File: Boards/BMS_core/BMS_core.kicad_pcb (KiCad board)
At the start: 2 copper layers, 31 parts, among them IC1 ATMEGA16M1, J1 CONN_02X03, T1 T_LAN_7490100111A, U1 MCP2561-E_SN, U101 TPS561201, Y1 Crystal_SMD

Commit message: Rev 1 Layout of BMS Core
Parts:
- added C10: C_0.1uF, footprints:C_0805_OEM, F.Cu at (107.6, 57.5)
- added C6: C_0.1uF, footprints:C_0805_OEM, F.Cu at (64.5, 81.8)
- added C7: C_0.1uF, footprints:C_0805_OEM, F.Cu at (97.3, 57.7)
- added C8: C_10nF, footprints:C_0805_OEM, F.Cu at (82.0, 104.6)
- added C9: C_10nF, footprints:C_0805_OEM, F.Cu at (85.6, 102.6)
- added D1: LED_0805, footprints:LED_0805_OEM, F.Cu at (77.0, 67.5)
- added D2: LED_0805, footprints:LED_0805_OEM, F.Cu at (77.0, 69.8)
- added D3: LED_0805, footprints:LED_0805_OEM, F.Cu at (77.0, 72.4)
- added D4: BAS40-00, Package_TO_SOT_SMD:SOT-23, F.Cu at (84.8, 59.2)
- added J2: B5B-PH-K-S, footprints:B5B-PH-K-S, F.Cu at (98.3, 52.6)
- added J3: NanoFit_2, footprints:NanoFit_Molex_1x02x2.50mm_Angled_OEM, F.Cu at (104.1, 95.2)
- added J4: MicroFit_RA_R_2, footprints:MicroFit_RA_2, F.Cu at (49.5, 57.1)
- added J5: MM_F_VT_14, footprints:micromatch_female_vert_14, F.Cu at (45.7, 72.4)
- added K1: G5Q-1A4-DC5-5V, footprints:Relay_SPST_OMRON-G5Q-1A4_OEM, F.Cu at (81.3, 52.1)
- added Q1: SSM3K333R, footprints:SOT-23F, F.Cu at (85.3, 52.7)
- added R10: R_60.4, footprints:R_0805_OEM, F.Cu at (85.6, 104.6)
- added R11: R_60.4, footprints:R_0805_OEM, F.Cu at (85.6, 100.6)
- added R12: R_10K, footprints:R_0805_OEM, F.Cu at (88.4, 52.7)
- added R13: R_17.4K_0.1, footprints:R_0805_OEM, F.Cu at (101.6, 61.7)
- added R14: R_1K_0.1, footprints:R_0805_OEM, F.Cu at (103.6, 61.7)
- added R4: R_200, footprints:R_0805_OEM, F.Cu at (73.3, 67.5)
- added R5: R_200, footprints:R_0805_OEM, F.Cu at (73.3, 69.8)
- added R6: R_200, footprints:R_0805_OEM, F.Cu at (73.3, 72.3)
- added R7: R_10K, footprints:R_0805_OEM, F.Cu at (91.1, 56.9)
- added R8: R_3.01K, footprints:R_0805_OEM, F.Cu at (82.5, 95.6)
- added R9: R_1K, footprints:R_0805_OEM, F.Cu at (80.7, 97.6)
- added REF**: Bolt_connect_4-40_round, footprints:Bolt_connect_4-40_round, F.Cu at (112.4, 52.7)
- added REF**: Bolt_connect_4-40_round, footprints:Bolt_connect_4-40_round, F.Cu at (47.6, 104.8)
- added REF**: Bolt_connect_4-40_round, footprints:Bolt_connect_4-40_round, F.Cu at (112.4, 104.8)
- added U2: SN74LVC1G17, Package_TO_SOT_SMD:SOT-23-5, F.Cu at (61.5, 81.8)
- added U3: LTC6820HMS, Package_SO:MSOP-16_3x4mm_P0.5mm, F.Cu at (79.4, 91.2)
- added U4: MCP6001, footprints:SOT-23-5_OEM, F.Cu at (100.3, 57.7)
- added U5: MCP6001, footprints:SOT-23-5_OEM, F.Cu at (107.5, 60.5)
- R104: value R_51.1K -> R_54.9K
- moved R3 89.2 mm to (53.3, 70.4), turned to 90 degrees
- moved U101 80.3 mm to (61.8, 102.7)
- moved C101 80.3 mm to (58.4, 103.0)
- moved C102 80.3 mm to (64.8, 104.0)
- moved C103 80.3 mm to (68.6, 93.3)
- moved C104 80.3 mm to (68.6, 95.4)
- moved C105 80.3 mm to (68.6, 97.7)
- moved D102 80.3 mm to (51.6, 95.6)
- moved L101 80.3 mm to (61.8, 96.1)
- moved R101 80.3 mm to (52.3, 99.2)
- moved R102 80.3 mm to (52.3, 101.2)
- moved R103 80.3 mm to (59.9, 106.3)
- moved D101 80.3 mm to (54.1, 89.0)
- moved D103 80.3 mm to (64.3, 86.5)
- moved F101 80.3 mm to (55.5, 96.8)
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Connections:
- net /12V_Fused renamed Net-(C101-Pad1)
- IC1 pad 13: Net-(IC1-Pad13) -> /PROG_1
- IC1 pad 14: Net-(IC1-Pad14) -> /PROG_2
- IC1 pad 15: Net-(IC1-Pad15) -> /PROG_3
- IC1 pad 16: Net-(IC1-Pad16) -> /~OCD
- IC1 pad 17: Net-(IC1-Pad17) -> /VREF
- IC1 pad 18: Net-(IC1-Pad18) -> /VOUT
- IC1 pad 22: /SensorAmp -> /BMS_SENSE
- IC1 pad 25: Net-(IC1-Pad25) -> /RELAY_DRIVE
- IC1 pad 27: Net-(IC1-Pad27) -> /CS_iso
- IC1 pad 28: Net-(IC1-Pad28) -> /SCK_iso
- IC1 pad 3: /SS -> /FAN_PWM_RAW
- IC1 pad 30: Net-(IC1-Pad30) -> /BSPD_CURRENT
- IC1 pad 8: Net-(IC1-Pad8) -> /MISO_iso
- IC1 pad 9: Net-(IC1-Pad9) -> /MOSI_iso
- R1 pad 1: Net-(R1-Pad1) -> VCC
- R104 pad 1: Net-(C103-Pad1) -> Net-(R103-Pad1)
- R104 pad 2: Net-(R103-Pad1) -> Net-(C103-Pad1)
- R3 pad 1: Net-(R3-Pad1) -> /CANH
- R3 pad 2: Net-(R3-Pad2) -> /CANL
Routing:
- net VCC: track 4.46 -> 212.2 mm, vias 0 -> 5
- net /VOUT: track 0.00 -> 81.4 mm, vias 0 -> 4
- net /BSPD_CURRENT: track 0.00 -> 78.4 mm, vias 0 -> 4
- net +12V: track 4.95 -> 79.7 mm
- net /MISO: track 0.00 -> 73.4 mm, vias 0 -> 3
- net /RESET: track 0.00 -> 70.8 mm, vias 0 -> 4
- net /MOSI: track 0.00 -> 69.8 mm, vias 0 -> 3
- net /SCK: track 0.00 -> 64.6 mm, vias 0 -> 5
- net /VREF: track 0.00 -> 59.5 mm, vias 0 -> 2
- net GND: track 14.4 -> 70.8 mm, vias 14 -> 39
- net /TXCAN: track 0.00 -> 52.1 mm
- net /RXCAN: track 0.00 -> 42.6 mm
- net /BMS_SENSE: track 0.00 -> 40.7 mm, vias 0 -> 2
- net /~OCD: track 0.00 -> 39.7 mm, vias 0 -> 2
- net /FAN_PWM_RAW: track 0.00 -> 35.6 mm, vias 0 -> 2
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- added copper zone on B.Cu, net GND
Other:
- board outline added: 73.7 x 61 mm
- board text added: "GLV"
- board text added: "HV"
- board text added: "MKIV BMS Core Rev 1.0 Olin Electric Motorsports Alexander Hoppe '19"
- board text added: "PD5"
- board text added: "PD6"
- board text added: "PD7"

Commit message: Add gerbers for BMS Core Rev.1
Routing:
- net /SHDN_OUT(BMS->IMD): track 0.00 -> 19.9 mm
- net /SHDN_IN(MAIN_PACK->BMS): track 0.00 -> 12.4 mm
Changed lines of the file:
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@@
     (thickness 1.6)
     (drawings 16)
-    (tracks 726)
+    (tracks 732)
     (zones 0)
     (modules 64)
@@
   )
   (setup
-    (last_trace_width 0.254)
+    (last_trace_width 0.762)
     (user_trace_width 0.1524)
     (user_trace_width 0.254)
@@
   (segment (start 77.654257 78.852742) (end 78.546757 77.960242) (width 0.254) (layer F.Cu) (net 15))
   (segment (start 77.654257 78.963742) (end 77.654257 78.852742) (width 0.254) (layer F.Cu) (net 15))
-  (segment (start 59.0101 101.5795) (end 58.9601 101.6295) (width 0.6) (layer F.Cu) (net 38) (status 30))
   (segment (start 54.2925 91.059) (end 54.102 91.059) (width 0.254) (layer F.Cu) (net 16))
   (segment (start 55.4795 92.246) (end 54.2925 91.059) (width 0.254) (layer F.Cu) (net 16))
@@
   (segment (start 83.82 104.648) (end 83.042 104.648) (width 0.254) (layer F.Cu) (net 36))
   (segment (start 90.26 102.616) (end 86.598 102.616) (width 0.254) (layer F.Cu) (net 37))
+  (segment (start 59.0101 101.5795) (end 58.9601 101.6295) (width 0.6) (layer F.Cu) (net 38) (status 30))
   (segment (start 78.700757 67.533742) (end 78.135257 67.533742) (width 0.254) (layer F.Cu) (net 39))
   (segment (start 84.255257 73.088242) (end 78.700757 67.533742) (width 0.254) (layer F.Cu) (net 39))
@@
   (segment (start 100.544 101.346) (end 99.06 101.346) (width 0.254) (layer F.Cu) (net 56))
   (segment (start 104.14 97.75) (end 100.544 101.346) (width 0.254) (layer F.Cu) (net 56))
-  (segment (start 101.536001 51.816001) (end 102.298 52.578) (width 0.254) (layer F.Cu) (net 69))
-  (segment (start 90.17 56.896) (end 90.17 54.864) (width 0.254) (layer F.Cu) (net 69))
-  (segment (start 90.17 54.864) (end 93.726 51.308) (width 0.254) (layer F.Cu) (net 69))
-  (segment (start 93.726 51.308) (end 101.028 51.308) (width 0.254) (layer F.Cu) (net 69))
-  (segment (start 101.028 51.308) (end 101.536001 51.816001) (width 0.254) (layer F.Cu) (net 69))
-  (segment (start 90.17 56.896) (end 90.17 60.452) (width 0.254) (layer F.Cu) (net 69))
-  (segment (start 90.17 60.452) (end 90.17 60.96) (width 0.254) (layer F.Cu) (net 69))
-  (via (at 84.074 62.23) (size 0.6096) (drill 0.3048) (layers F.Cu B.Cu) (net 69))
-  (segment (start 90.17 60.96) (end 88.9 62.23) (width 0.254) (layer F.Cu) (net 69))
-  (segment (start 88.9 62.23) (end 84.074 62.23) (width 0.254) (layer F.Cu) (net 69))
-  (segment (start 84.074 62.23) (end 84.074 62.992) (width 0.254) (layer B.Cu) (net 69))
-  (segment (start 84.074 62.992) (end 81.788 65.278) (width 0.254) (layer B.Cu) (net 69))
-  (via (at 81.788 72.644) (size 0.6096) (drill 0.3048) (layers F.Cu B.Cu) (net 69))
-  (segment (start 81.788 65.278) (end 81.788 72.644) (width 0.254) (layer B.Cu) (net 69))
+  (segment (start 56.92 58.65) (end 53.85 58.65) (width 0.762) (layer F.Cu) (net 57))
+  (segment (start 63.5 52.07) (end 56.92 58.65) (width 0.762) (layer F.Cu) (net 57))
+  (segment (start 54.559999 54.940001) (end 53.85 55.65) (width 0.762) (layer F.Cu) (net 58))
+  (segment (start 58.863401 50.636599) (end 54.559999 54.940001) (width 0.762) (layer F.Cu) (net 58))
+  (segment (start 69.686599 50.636599) (end 58.863401 50.636599) (width 0.762) (layer F.Cu) (net 58))
+  (segment (start 71.12 52.07) (end 69.686599 50.636599) (width 0.762) (layer F.Cu) (net 58))
   (segment (start 48.26 82.296) (end 50.292 84.328) (width 0.254) (layer F.Cu) (net 61))
   (segment (start 50.292 84.328) (end 56.642 84.328) (width 0.254) (layer F.Cu) (net 61))
@@
   (segment (start 81.959166 52.749166) (end 81.28 52.07) (width 0.762) (layer F.Cu) (net 68))
   (segment (start 84.294147 52.749166) (end 81.959166 52.749166) (width 0.762) (layer F.Cu) (net 68))
+  (segment (start 101.536001 51.816001) (end 102.298 52.578) (width 0.254) (layer F.Cu) (net 69))
+  (segment (start 90.17 56.896) (end 90.17 54.864) (width 0.254) (layer F.Cu) (net 69))
+  (segment (start 90.17 54.864) (end 93.726 51.308) (width 0.254) (layer F.Cu) (net 69))
+  (segment (start 93.726 51.308) (end 101.028 51.308) (width 0.254) (layer F.Cu) (net 69))
+  (segment (start 101.028 51.308) (end 101.536001 51.816001) (width 0.254) (layer F.Cu) (net 69))
+  (segment (start 90.17 56.896) (end 90.17 60.452) (width 0.254) (layer F.Cu) (net 69))
+  (segment (start 90.17 60.452) (end 90.17 60.96) (width 0.254) (layer F.Cu) (net 69))
+  (via (at 84.074 62.23) (size 0.6096) (drill 0.3048) (layers F.Cu B.Cu) (net 69))
+  (segment (start 90.17 60.96) (end 88.9 62.23) (width 0.254) (layer F.Cu) (net 69))
+  (segment (start 88.9 62.23) (end 84.074 62.23) (width 0.254) (layer F.Cu) (net 69))
+  (segment (start 84.074 62.23) (end 84.074 62.992) (width 0.254) (layer B.Cu) (net 69))
+  (segment (start 84.074 62.992) (end 81.788 65.278) (width 0.254) (layer B.Cu) (net 69))
+  (via (at 81.788 72.644) (size 0.6096) (drill 0.3048) (layers F.Cu B.Cu) (net 69))
+  (segment (start 81.788 65.278) (end 81.788 72.644) (width 0.254) (layer B.Cu) (net 69))
   (segment (start 81.855257 72.711257) (end 81.788 72.644) (width 0.254) (layer F.Cu) (net 69))
   (segment (start 81.855257 74.142242) (end 81.855257 72.711257) (width 0.254) (layer F.Cu) (net 69))

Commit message: Add silkscreens and update gerbers for rev 1
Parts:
- added G***: LOGO, footprints:Olin_O, B.Cu at (92.3, 55.9)
- moved G*** 78.5 mm to (80.8, 102.8), turned to 180 degrees
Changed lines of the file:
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@@
     (tracks 732)
     (zones 0)
-    (modules 64)
+    (modules 65)
     (nets 70)
   )
@@
     (34 B.Paste user)
     (35 F.Paste user)
-    (36 B.SilkS user hide)
+    (36 B.SilkS user)
     (37 F.SilkS user)
-    (38 B.Mask user)
+    (38 B.Mask user hide)
     (39 F.Mask user hide)
     (40 Dwgs.User user)
@@
   )
   (setup
-    (last_trace_width 0.762)
+    (last_trace_width 0.1524)
     (user_trace_width 0.1524)
     (user_trace_width 0.254)
@@
       (drillshape 0)
       (scaleselection 1)
-      (outputdirectory "Gerb_new/"))
+      (outputdirectory "gerbers/"))
   )
   (net 0 "")
@@
   )
   (module footprints:Logo_Large (layer B.Cu)
-    (at 159.004 109.728)
-    (fp_text reference G*** (at 0 0) (layer B.SilkS) hide
+    (at 80.8482 102.7938 180)
+    (fp_text reference G*** (at 0 0 180) (layer B.SilkS) hide
       (effects (font (size 1.524 1.524) (thickness 0.3)) (justify mirror))
     )
-    (fp_text value LOGO (at 0.75 0) (layer B.SilkS) hide
+    (fp_text value LOGO (at 0.75 0 180) (layer B.SilkS) hide
       (effects (font (size 1.524 1.524) (thickness 0.3)) (justify mirror))
     )
@@
       (clearance 0.508))
   )
+  (module footprints:Olin_O (layer B.Cu)
+    (at 92.329 55.8546)
+    (fp_text reference G*** (at 10.16 5.08) (layer B.SilkS) hide
+      (effects (font (size 1.524 1.524) (thickness 0.3)) (justify mirror))
+    )
+    (fp_text value LOGO (at 10.16 7.62) (layer B.SilkS) hide
+      (effects (font (size 1.524 1.524) (thickness 0.3)) (justify mirror))
+    )
+    (fp_poly (pts (xy 0.78907 2.933726) (xy 0.297169 2.603291) (xy -0.249654 2.169905) (xy -0.811 1.670573)
+      (xy -1.346471 1.1423) (xy -1.815667 0.622091) (xy -2.036037 0.345931) (xy -2.493304 -0.320664)
+      (xy -2.866143 -0.986545) (xy -3.148527 -1.632052) (xy -3.33443 -2.237523) (xy -3.417825 -2.783297)
+      (xy -3.392687 -3.249711) (xy -3.252989 -3.617104) (xy -3.251451 -3.6195) (xy -3.169272 -3.757194)
+      (xy -3.151881 -3.805837) (xy -3.238357 -3.784085) (xy -3.451232 -3.729169) (xy -3.753084 -3.650766)
+      (xy -3.937 -3.602827) (xy -4.929803 -3.301284) (xy -5.762117 -2.955854) (xy -6.437575 -2.564339)
+      (xy -6.959808 -2.124543) (xy -7.332449 -1.634266) (xy -7.40086 -1.507176) (xy -7.582592 -0.976433)
+      (xy -7.604253 -0.451032) (xy -7.475103 0.063274) (xy -7.204403 0.560731) (xy -6.801416 1.035585)
+      (xy -6.275401 1.482082) (xy -5.63562 1.894469) (xy -4.891334 2.266991) (xy -4.051805 2.593894)
+      (xy -3.126293 2.869426) (xy -2.12406 3.087831) (xy -1.054367 3.243355) (xy 0.073526 3.330246)
+      (xy 0.403482 3.341618) (xy 1.526631 3.369785) (xy 0.78907 2.933726)) (layer B.SilkS) (width 0.01))
+    (fp_poly (pts (xy 3.442983 3.189143) (xy 3.593457 3.149129) (xy 3.859628 3.080824) (xy 4.192829 2.996675)
+      (xy 4.318 2.965353) (xy 4.950523 2.771412) (xy 5.589166 2.511366) (xy 6.187709 2.208074)
+      (xy 6.699928 1.884399) (xy 7.006464 1.635631) (xy 7.427728 1.15255) (xy 7.68721 0.655705)
+      (xy 7.791208 0.151883) (xy 7.746021 -0.352128) (xy 7.557949 -0.849541) (xy 7.23329 -1.333569)
+      (xy 6.778343 -1.797426) (xy 6.199408 -2.234324) (xy 5.502783 -2.637476) (xy 4.694767 -3.000096)
+      (xy 3.78166 -3.315395) (xy 2.769759 -3.576588) (xy 2.037525 -3.718298) (xy 1.579989 -3.791873)
+      (xy 1.263227 -3.832252) (xy 1.062288 -3.841026) (xy 0.952225 -3.819783) (xy 0.916988 -3.789688)
+      (xy 0.858074 -3.735928) (xy 0.847963 -3.779733) (xy 0.766319 -3.839404) (xy 0.537525 -3.878973)
+      (xy 0.3175 -3.891838) (xy -0.049381 -3.903054) (xy -0.420533 -3.915266) (xy -0.613858 -3.922106)
+      (xy -0.848176 -3.919314) (xy -0.993137 -3.895498) (xy -1.016025 -3.876157) (xy -1.081706 -3.846379)
+      (xy -1.164166 -3.861997) (xy -1.171663 -3.848862) (xy -1.054877 -3.771153) (xy -0.838402 -3.644985)
+      (xy -0.801282 -3.624227) (xy -0.008948 -3.11414) (xy 0.773964 -2.467576) (xy 1.356472 -1.894766)
+      (xy 2.033545 -1.129263) (xy 2.578075 -0.383663) (xy 3.016751 0.379744) (xy 3.126149 0.605915)
+      (xy 3.414204 1.311966) (xy 3.572957 1.91735) (xy 3.603305 2.429665) (xy 3.50615 2.856508)
+      (xy 3.413505 3.034819) (xy 3.334494 3.173405) (xy 3.358577 3.208225) (xy 3.442983 3.189143)) (layer B.SilkS) (width 0.01))
+  )
   (gr_arc (start 45.72 106.68) (end 43.18 106.68) (angle -90) (layer Edge.Cuts) (width 0.15))

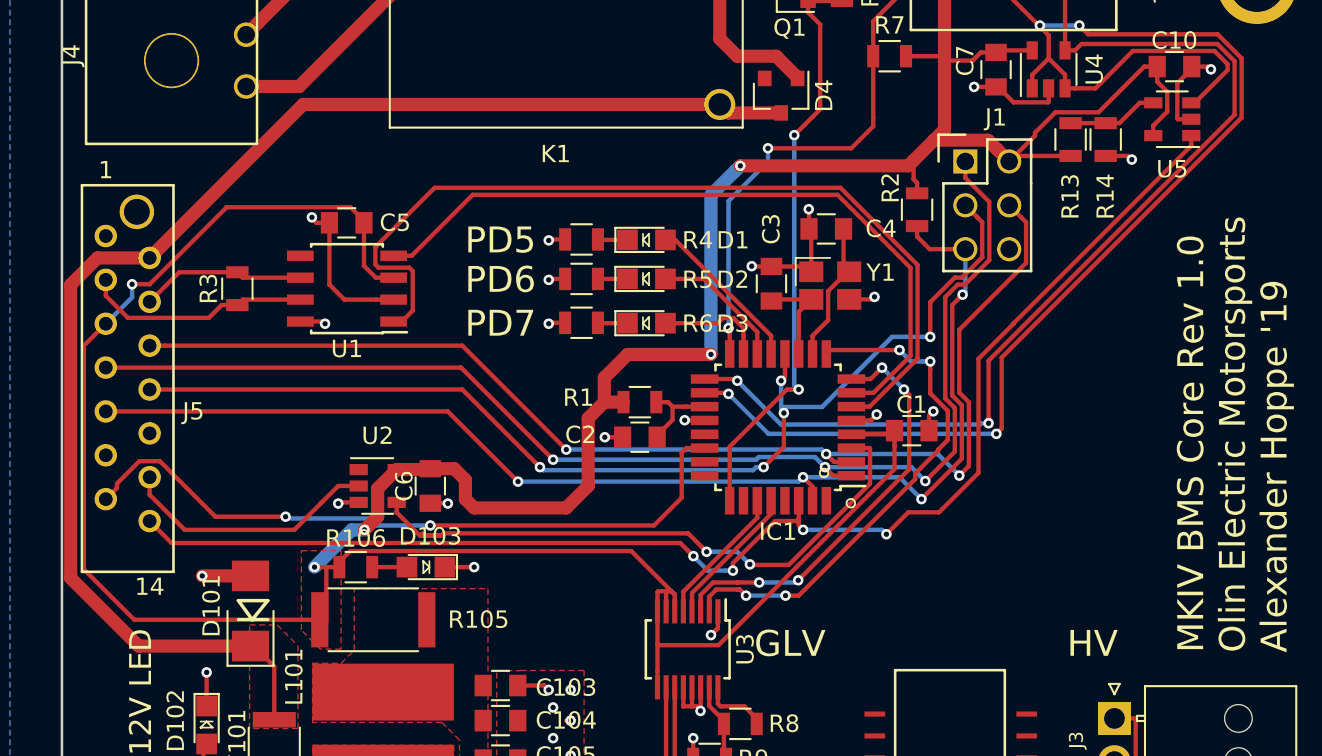
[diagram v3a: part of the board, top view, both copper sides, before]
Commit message: Update BMS Core with LED1 and LED2 connections
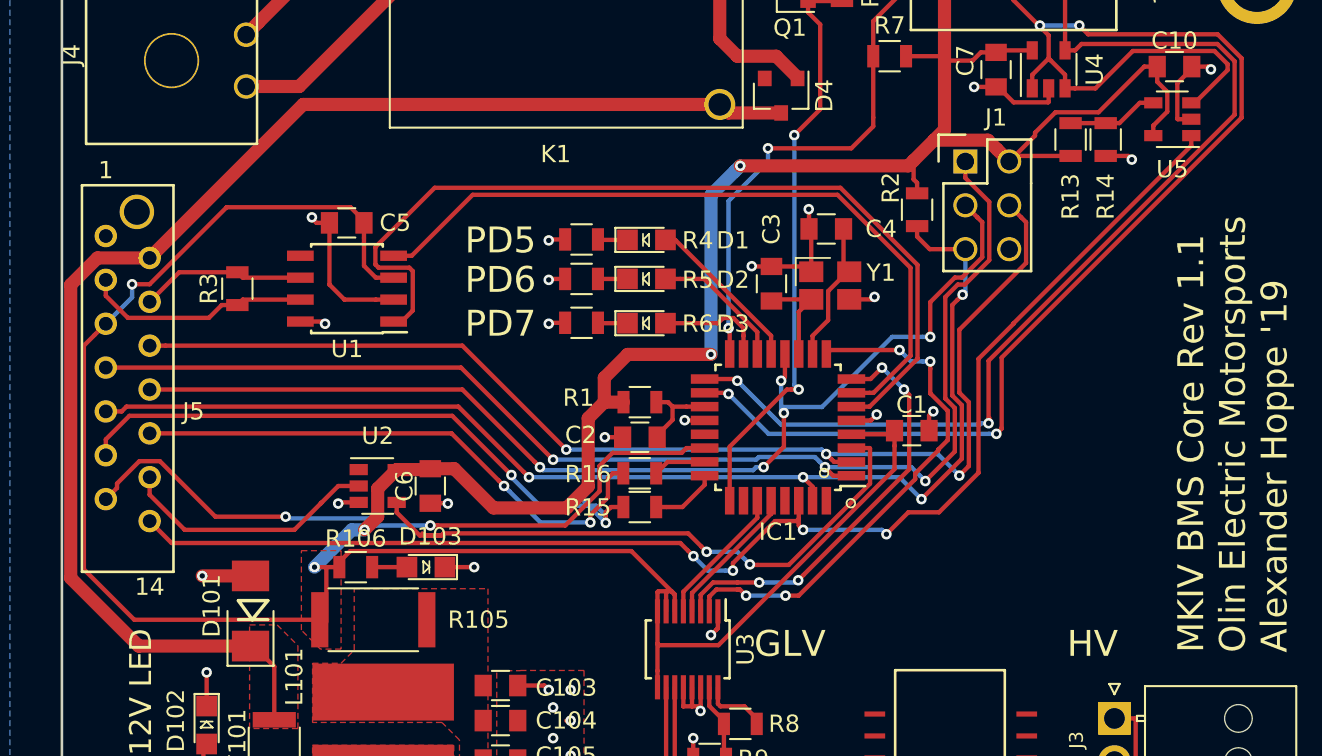
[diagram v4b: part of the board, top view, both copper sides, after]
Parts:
- added R15: R_200, footprints:R_0805_OEM, F.Cu at (76.6, 83.0)
- added R16: R_200, footprints:R_0805_OEM, F.Cu at (76.6, 81.1)
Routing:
- net /RJ45_LED2: track 0.00 -> 37.1 mm, vias 0 -> 2
- net /RJ45_LED1: track 0.00 -> 31.7 mm, vias 0 -> 2
- net Net-(IC1-Pad24): track 0.00 -> 3.87 mm
- net Net-(IC1-Pad23): track 0.00 -> 3.08 mm
- net /BMS_SENSE: track 40.7 -> 40.0 mm
- net VCC: track 212.2 -> 211.6 mm
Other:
- board text added: "MKIV BMS Core Rev 1.1 Olin Electric Motorsports Alexander Hoppe '19"
- board text removed: "MKIV BMS Core Rev 1.0 Olin Electric Motorsports Alexander Hoppe '19"
